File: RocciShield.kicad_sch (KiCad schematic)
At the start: 182 parts, among them J1 Battery, J10 M3, J11 I2C6, J12 M4, J13 I2C7, J14 Power, J2 I2C0, J3 I2C1, J4 I2C2, J5 I2C3, J6 M1, J7 I2C4, J8 M2, J9 I2C5, Q1 IRF7416, Q2 2N7002, U1 LMR33630, U10 LM317_TO-252, U2 LM317_TO-252, U4 TPS3700, U5 TCA9548A, U6 DRV8871, U7 DRV8871, U8 DRV8871, U9 DRV8871

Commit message: added changes from #2
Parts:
- removed C11, C12, C14, C15, C16, C17, C18, C3, C6, C8, C9: 100n, Capacitor_SMD:C_0603_1608Metric, symbol Device:C_Polarized
- removed C2: 220n, Capacitor_SMD:C_0603_1608Metric, symbol Device:C_Polarized
- removed C7: 1µ, Capacitor_SMD:CP_Elec_5x3, symbol Device:C_Polarized
- added C11, C12, C14, C15, C16, C17, C18, C19, C3, C6, C8, C9: 100n, Capacitor_SMD:C_0603_1608Metric, symbol Device:C
- added C2: 220n, Capacitor_SMD:C_0603_1608Metric, symbol Device:C
- added C7: 1µ, Capacitor_SMD:C_0603_1608Metric, symbol Device:C
- C1: value 22µ -> 33µ; footprint Capacitor_SMD:CP_Elec_5x3 -> Capacitor_Tantalum_SMD:CP_EIA-7343-43_Kemet-X; LSCL (none) -> C542504
- C10: value 22 µF -> 33µ; footprint Capacitor_SMD:CP_Elec_5x3 -> Capacitor_Tantalum_SMD:CP_EIA-7343-43_Kemet-X
- C13: value 22µ -> 33µ; footprint Capacitor_SMD:C_0603_1608Metric -> Capacitor_Tantalum_SMD:CP_EIA-7343-43_Kemet-X; LSCL (none) -> C3009395
- C4: value 22 µF -> 33µ; footprint Capacitor_SMD:CP_Elec_5x3 -> Capacitor_Tantalum_SMD:CP_EIA-7343-43_Kemet-X; LSCL C347540 -> C3009395
- C5: value 22 µF -> 33µ; footprint Capacitor_SMD:CP_Elec_5x3 -> Capacitor_Tantalum_SMD:CP_EIA-7343-43_Kemet-X; LSCL (none) -> C3009395
- D26: renamed from D31; footprint LED_SMD:LED_0603_1608Metric -> Diode_SMD:D_MiniMELF; LCSC C72043 -> C8056
- D27: renamed from D30; footprint LED_SMD:LED_0603_1608Metric -> Diode_SMD:D_MiniMELF; LCSC C72043 -> C8062
- F1: value 1 A -> 300 mA ptc; LSCL (none) -> C261938
- F10: renamed from F23; value 1 A -> 300 mA ptc
- F11: renamed from F27; value 1A -> 1A ptc; footprint Fuse:Fuse_1812_4532Metric -> Fuse:Fuse_1206_3216Metric; LSCL (none) -> C910830
- F3: renamed from F5; value 1 A -> 300 mA ptc
- F4: renamed from F8; value 1 A -> 300 mA ptc
- F5: renamed from F11; value 1 A -> 300 mA ptc
- F6: renamed from F14; value 1 A -> 300 mA ptc
- F7: renamed from F17; value 1 A -> 300 mA ptc
- F8: renamed from F20; value 1 A -> 300 mA ptc
- F9: renamed from F26; value 3A -> 3A ptc; footprint Fuse:Fuse_1812_4532Metric -> Fuse:Fuse_2920_7451Metric; LSCL (none) -> C2977527
- L1: footprint Inductor_SMD:L_6.3x6.3_H3 -> Inductor_SMD:L_Sunlord_SWPA4020S
- Q2: footprint (none) -> Package_TO_SOT_SMD:SOT-23
- R12: renamed from R44; footprint (none) -> Resistor_SMD:R_0603_1608Metric
- R13: renamed from R10; value 383k 1% -> 4700k 1%
- R15: renamed from R45; footprint (none) -> Resistor_SMD:R_0603_1608Metric
- R19: renamed from R15; value 1k47 1% -> 10k 1%
- R20: renamed from R59; footprint (none) -> Resistor_SMD:R_0603_1608Metric
- R21: renamed from R61; footprint (none) -> Resistor_SMD:R_0603_1608Metric
- R24: renamed from R58; footprint (none) -> Resistor_SMD:R_0603_1608Metric
- R25: renamed from R60; footprint (none) -> Resistor_SMD:R_0603_1608Metric
- R26: renamed from R18; value 14k3 1% -> 180k 1%
- R27: renamed from R46; footprint (none) -> Resistor_SMD:R_0603_1608Metric
- R28: renamed from R47; footprint (none) -> Resistor_SMD:R_0603_1608Metric
- R3: renamed from R42; footprint (none) -> Resistor_SMD:R_0603_1608Metric
- R31: renamed from R48; footprint (none) -> Resistor_SMD:R_0603_1608Metric
- R32: renamed from R49; footprint (none) -> Resistor_SMD:R_0603_1608Metric
- R35: renamed from R23; footprint Resistor_SMD:R_0603_1608Metric -> Resistor_SMD:R_0805_2012Metric
- R38: renamed from R50; footprint (none) -> Resistor_SMD:R_0603_1608Metric
- R39: renamed from R51; footprint (none) -> Resistor_SMD:R_0603_1608Metric
- R4: renamed from R43; footprint (none) -> Resistor_SMD:R_0603_1608Metric
- R43: renamed from R29; footprint Resistor_SMD:R_0603_1608Metric -> Resistor_SMD:R_0805_2012Metric
- R47: renamed from R52; footprint (none) -> Resistor_SMD:R_0603_1608Metric
- R48: renamed from R53; footprint (none) -> Resistor_SMD:R_0603_1608Metric
- R51: renamed from R34; footprint Resistor_SMD:R_0603_1608Metric -> Resistor_SMD:R_0805_2012Metric
- R54, R55: footprint (none) -> Resistor_SMD:R_0603_1608Metric
- R58: renamed from R39; footprint Resistor_SMD:R_0603_1608Metric -> Resistor_SMD:R_0805_2012Metric
- R61: renamed from R56; footprint (none) -> Resistor_SMD:R_0603_1608Metric
- R62: renamed from R57; footprint (none) -> Resistor_SMD:R_0603_1608Metric
- renumbered D26 to D28, D27 to D29, D28 to D30, D29 to D31, D8 to D6, D6 to D7, D7 to D8, J14 to J12, J12 to J13, J13 to J14, R8 to R10, R9 to R11, R11 to R14, R14 to R16, R12 to R17, R13 to R18, R16 to R22, R17 to R23, R19 to R29, R20 to R30, R21 to R33, R22 to R34, R24 to R36, R25 to R37, R28 to R40, R26 to R41, R27 to R42, R30 to R44, R31 to R45, R62 to R46, R32 to R49, R3 to R5, R33 to R50, R35 to R52, R36 to R53, R37 to R56, R38 to R57, R40 to R59, R4 to R6, R41 to R60, R5 to R7, R6 to R8, R7 to R9, U10 to U3
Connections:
- net +12V: now also C14.1, C15.1, C16.1, C17.1, C2.1, C9.1
- net +3V3: now also C11.1
- net +5V: now also C6.1, C8.1
- net +8V: now also C12.1, C18.1
- net 12V_after_fuse: now also C19.1
- net Boot: now also C3.1
- net GND: now also C11.2, C12.2, C14.2, C15.2, C16.2, C17.2, C18.2, C19.2, C2.2, C6.2, C7.2, C8.2, C9.2
- net SW: now also C3.2
- net at R6.1, TP4.1, U1.6 (VCC): now also C7.1
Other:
- note added: "at 10,3 V it turns off at 10,8 V it turns on again See TPS3700_Lipo_protection_calc.xlsx for reference"
- note removed: "at 10,8 V it turns off at 11 V it turns on again"

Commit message: finished JLCPCB selection and fixed isse #3
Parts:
- removed Q1: IRF7416, Package_SO:SO-8_5.3x6.2mm_P1.27mm, symbol Device:Q_PMOS_GDS
- removed Q2: 2N7002, Package_TO_SOT_SMD:SOT-23, symbol Device:Q_NMOS_GDS
- added C19: 100n, Capacitor_SMD:C_0603_1608Metric, symbol Device:C
- added Q1: IRF7404, Package_SO:SOIC-8_3.9x4.9mm_P1.27mm, symbol Transistor_FET:IRF7404
- added Q2: 2N7002, Package_TO_SOT_SMD:SOT-23, symbol Device:Q_NMOS_GSD
- added R29: 300k 1%, Resistor_SMD:R_0603_1608Metric, symbol Device:R
- added R32: 100k 1%, Resistor_SMD:R_0603_1608Metric, symbol Device:R
- C1: value 33µ -> 100µ; footprint Capacitor_Tantalum_SMD:CP_EIA-7343-43_Kemet-X -> Package_TO_SOT_SMD:SOT-23; LCSC (none) -> C962164; LSCL C542504 -> C962164
- C10: renamed from C11; LCSC (none) -> C14663
- C11: renamed from C10; value 33µ -> 100µ; footprint Capacitor_Tantalum_SMD:CP_EIA-7343-43_Kemet-X -> Capacitor_SMD:CP_Elec_6.3x7.7; LCSC (none) -> C962164; LSCL (none) -> C962164
- C12: renamed from C9; LCSC (none) -> C14663
- C13: renamed from C12; LCSC (none) -> C14663
- C14: renamed from C13; value 33µ -> 100µ; footprint Capacitor_Tantalum_SMD:CP_EIA-7343-43_Kemet-X -> Capacitor_SMD:CP_Elec_6.3x7.7; LCSC (none) -> C962164; LSCL C3009395 -> C962164
- C15: renamed from C14; LCSC (none) -> C14663
- C16: renamed from C15; LCSC (none) -> C14663
- C17: renamed from C16; LCSC (none) -> C14663
- C18: renamed from C17; LCSC (none) -> C14663
- C2: LCSC (none) -> C21120
- C20: renamed from C18; LCSC (none) -> C14663
- C3, C6: LCSC (none) -> C14663
- C4, C5: LCSC (none) -> C3009395
- C7: LCSC (none) -> C15849
- C8: renamed from C19; LCSC (none) -> C14663
- C9: renamed from C8; LCSC (none) -> C14663
- F1, F10, F3, F4, F5, F6, F7, F8: LCSC (none) -> C261938
- F11: LCSC (none) -> C910830
- F9: LCSC (none) -> C2977527
- R1, R10, R11, R2, R22, R23, R8, R9: LCSC (none) -> C23162
- R12, R15, R27, R28, R3, R4: LCSC (none) -> C22775
- R13: LCSC (none) -> C23163
- R14, R19: LCSC (none) -> C25804
- R16: LCSC (none) -> C1603
- R17: LCSC (none) -> C23138
- R18: LCSC (none) -> C22808
- R20, R21: LCSC (none) -> C23350
- R24: LCSC (none) -> C23151
- R25: LCSC (none) -> C22767
- R26: LCSC (none) -> C22827
- R30: renamed from R29; LCSC (none) -> C23162
- R31: renamed from R30; LCSC (none) -> C23162
- R33: renamed from R31; LCSC (none) -> C22775
- R34: renamed from R32; LCSC (none) -> C22775
- R35: renamed from R33; LCSC (none) -> C1603
- R36: renamed from R34; LCSC (none) -> C1603
- R37: renamed from R35; LCSC (none) -> C22984
- R38: renamed from R36; LCSC (none) -> C23162
- R39: renamed from R37; LCSC (none) -> C23162
- R40: renamed from R38; LCSC (none) -> C22775
- R41: renamed from R39; LCSC (none) -> C22775
- R42: renamed from R40; LCSC (none) -> C22966
- R43: renamed from R41; LCSC (none) -> C1603
- R44: renamed from R42; LCSC (none) -> C1603
- R45: renamed from R43; LCSC (none) -> C22984
- R46: renamed from R44; LCSC (none) -> C23162
- R47: renamed from R45; LCSC (none) -> C23162
- R48: renamed from R46; value 1k -> 10k; LCSC (none) -> C25804
- R49: renamed from R47; LCSC (none) -> C22775
- R5, R6: LCSC (none) -> C25803
- R50: renamed from R48; LCSC (none) -> C22775
- R51: renamed from R49; LCSC (none) -> C1603
- R52: renamed from R50; LCSC (none) -> C1603
- R53: renamed from R51; LCSC (none) -> C22984
- R54: renamed from R52; LCSC (none) -> C23162
- R55: renamed from R53; LCSC (none) -> C23162
- R56: renamed from R54; LCSC (none) -> C22775
- R57: renamed from R55; LCSC (none) -> C22775
- R58: renamed from R56; LCSC (none) -> C1603
- R59: renamed from R57; LCSC (none) -> C1603
- R60: renamed from R58; LCSC (none) -> C22984
- R61: renamed from R59; LCSC (none) -> C23162
- R62: renamed from R60; LCSC (none) -> C23162
- R63: renamed from R61; LCSC (none) -> C22775
- R64: renamed from R62; LCSC (none) -> C22775
- R7: LCSC (none) -> C25962
- U2, U3: LCSC (none) -> C75510
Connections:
- net 12V_after_fuse is gone; now on net +12V: C8.1, D3.1 (K), F2.2, R13.1, R14.1, TP7.1, U4.5 (VDD)
- net +12V: now also Q1.5 (D), Q1.6 (D), Q1.7 (D), Q1.8 (D); no longer C1.1, C12.1, C2.1, D6.2 (A), U1.2 (VIN), U1.3 (EN), U3.3 (VI)
- net ADC_BAT: now also C19.2, R29.2, R32.1; no longer R13.2, R19.1, U4.3 (INA+)
- net ERROR_LED: now also Q2.1 (G)
- net GND: now also C19.1, Q2.3 (D), R32.2
- net at R14.2, TP13.1, U4.6 (OUTB): now also Q1.4 (G)
- net at R42.2: now also Q2.2 (S)
- new net: R13.2, R19.1, U4.3 (INA+)
- new net +12VA: C1.1, C12.1, C2.1, D6.2 (A), Q1.1 (S), Q1.2 (S), Q1.3 (S), R29.1, U1.2 (VIN), U1.3 (EN), U3.3 (VI)
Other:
- note added: "25V 50mΩ"
- note added: "3.15V @ 12.6 V 2.6V @ 10.4 V with VREF=5V -> span=110 ADU with VREF=3.3V -> span=167 ADU"
- note added: "30mΩ 5.2A"
- note added: "50V 340mΩ"
- note added: "TODO: - is the power connector large enough? - do we need max motor current?"
- note removed: "TODO: - select components for switching regulator - define netclasses - is the power connector large enough? - do we need max motor current? - add freerunning diodes"
- moved on the sheet: C2, C8

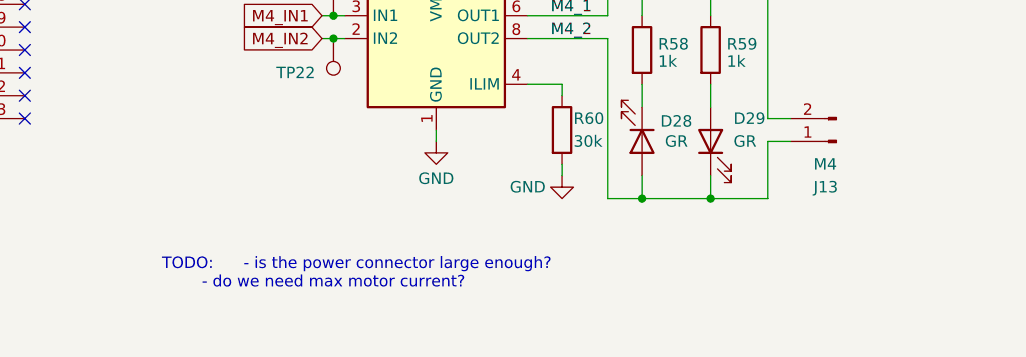
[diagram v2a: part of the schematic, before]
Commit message: added more TODOs
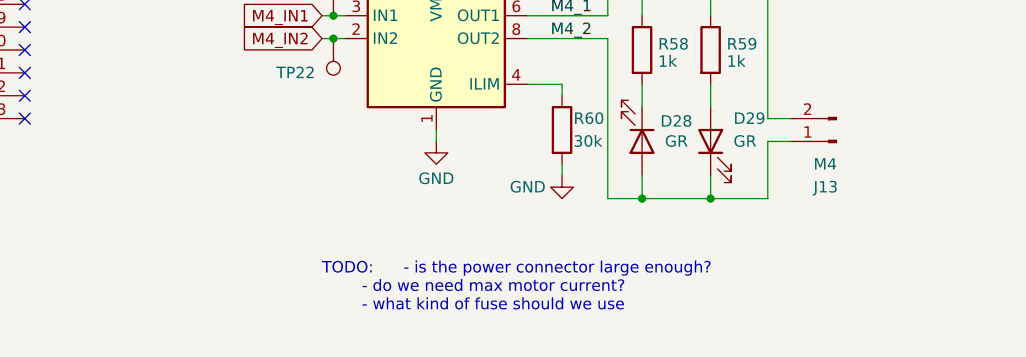
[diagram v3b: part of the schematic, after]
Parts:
- F2: LCSC (none) -> C122783
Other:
- note added: "TODO: - is the power connector large enough? - do we need max motor current? - what kind of fuse should we use"
- note removed: "TODO: - is the power connector large enough? - do we need max motor current?"
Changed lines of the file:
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@@
     (title "RoCCI Shield")
     (date "2023-06-27")
-    (rev "0.5")
+    (rev "0.6")
     (company "RoCCI e.V.")
   )
@@
     (effects (font (size 3 3)) (justify left bottom))
   )
-  (text "TODO:  	- is the power connector large enough?\n		- do we need max motor current?"
-    (at 302.26 257.81 0)
+  (text "TODO:  	- is the power connector large enough?\n		- do we need max motor current?\n		- what kind of fuse should we use "
+    (at 320.04 260.35 0)
     (effects (font (size 1.27 1.27)) (justify left bottom))
   )
@@
       (effects (font (size 1.27 1.27)) hide)
     )
+    (property "LCSC" "C122783" (at 213.36 34.29 90)
+      (effects (font (size 1.27 1.27)) hide)
+    )

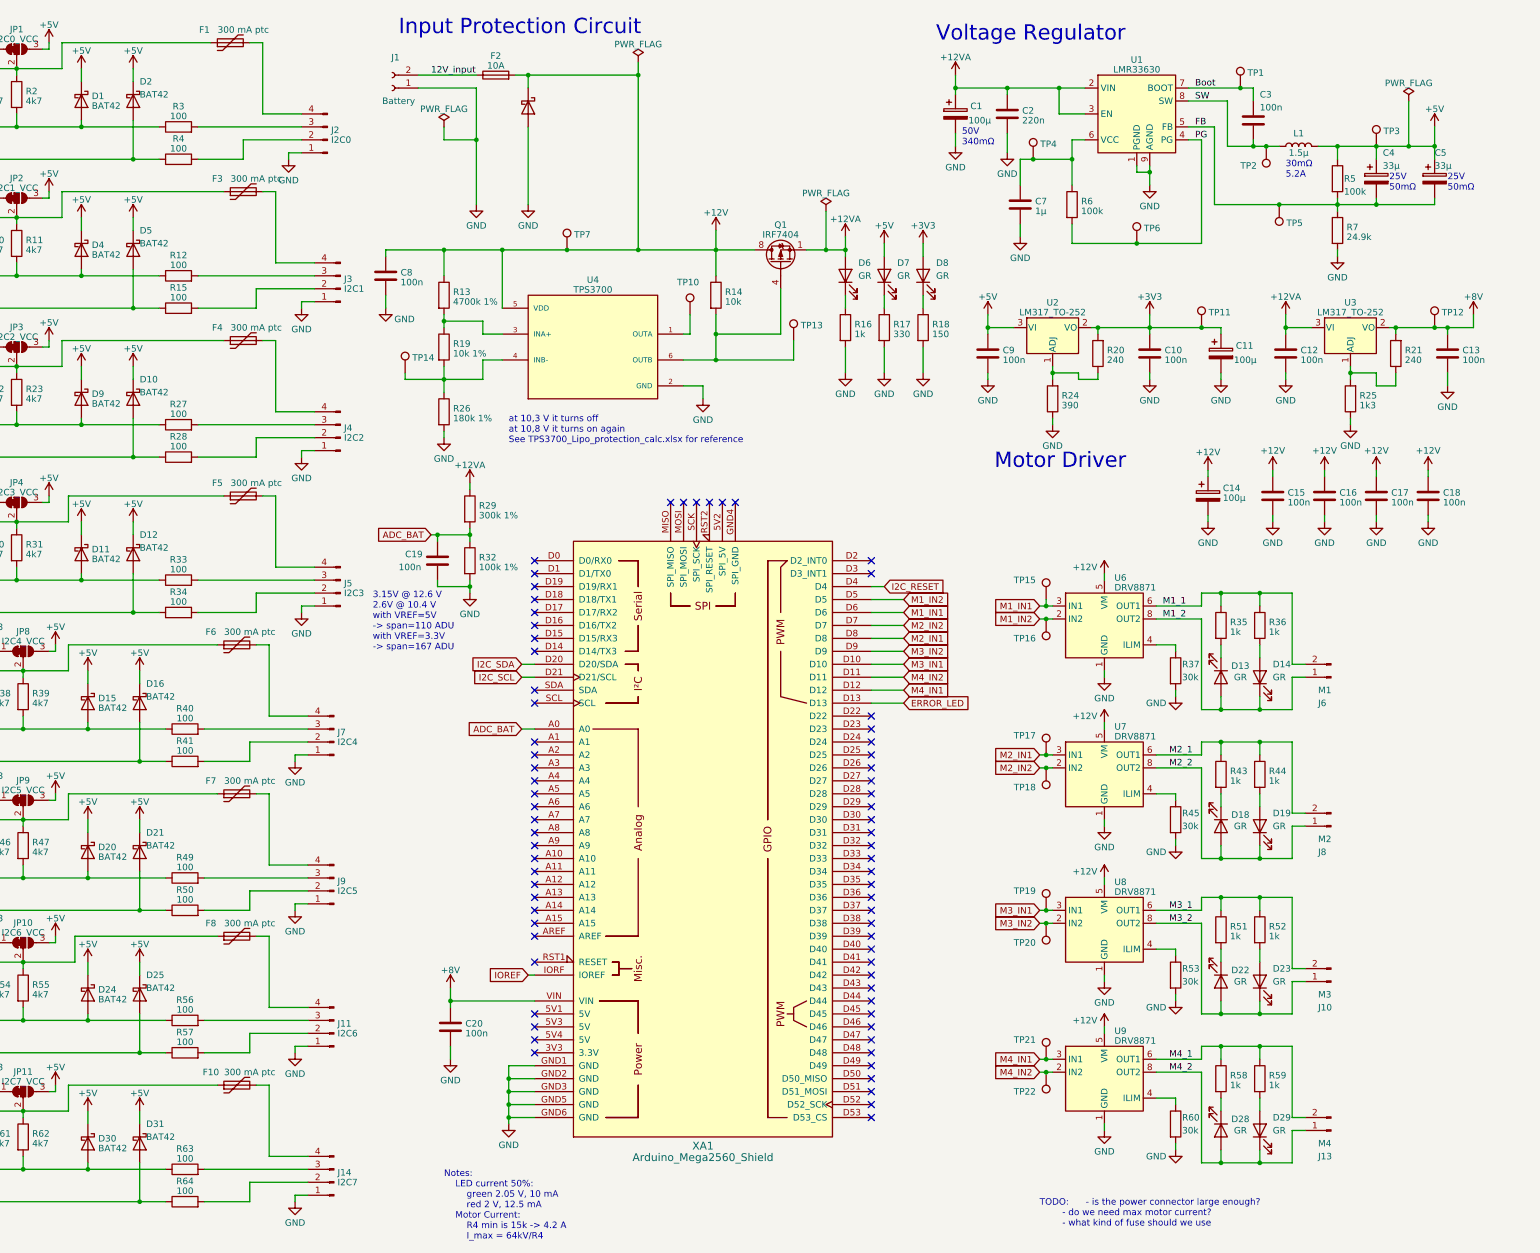
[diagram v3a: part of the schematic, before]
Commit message: first placment finished. Needs some adjustment
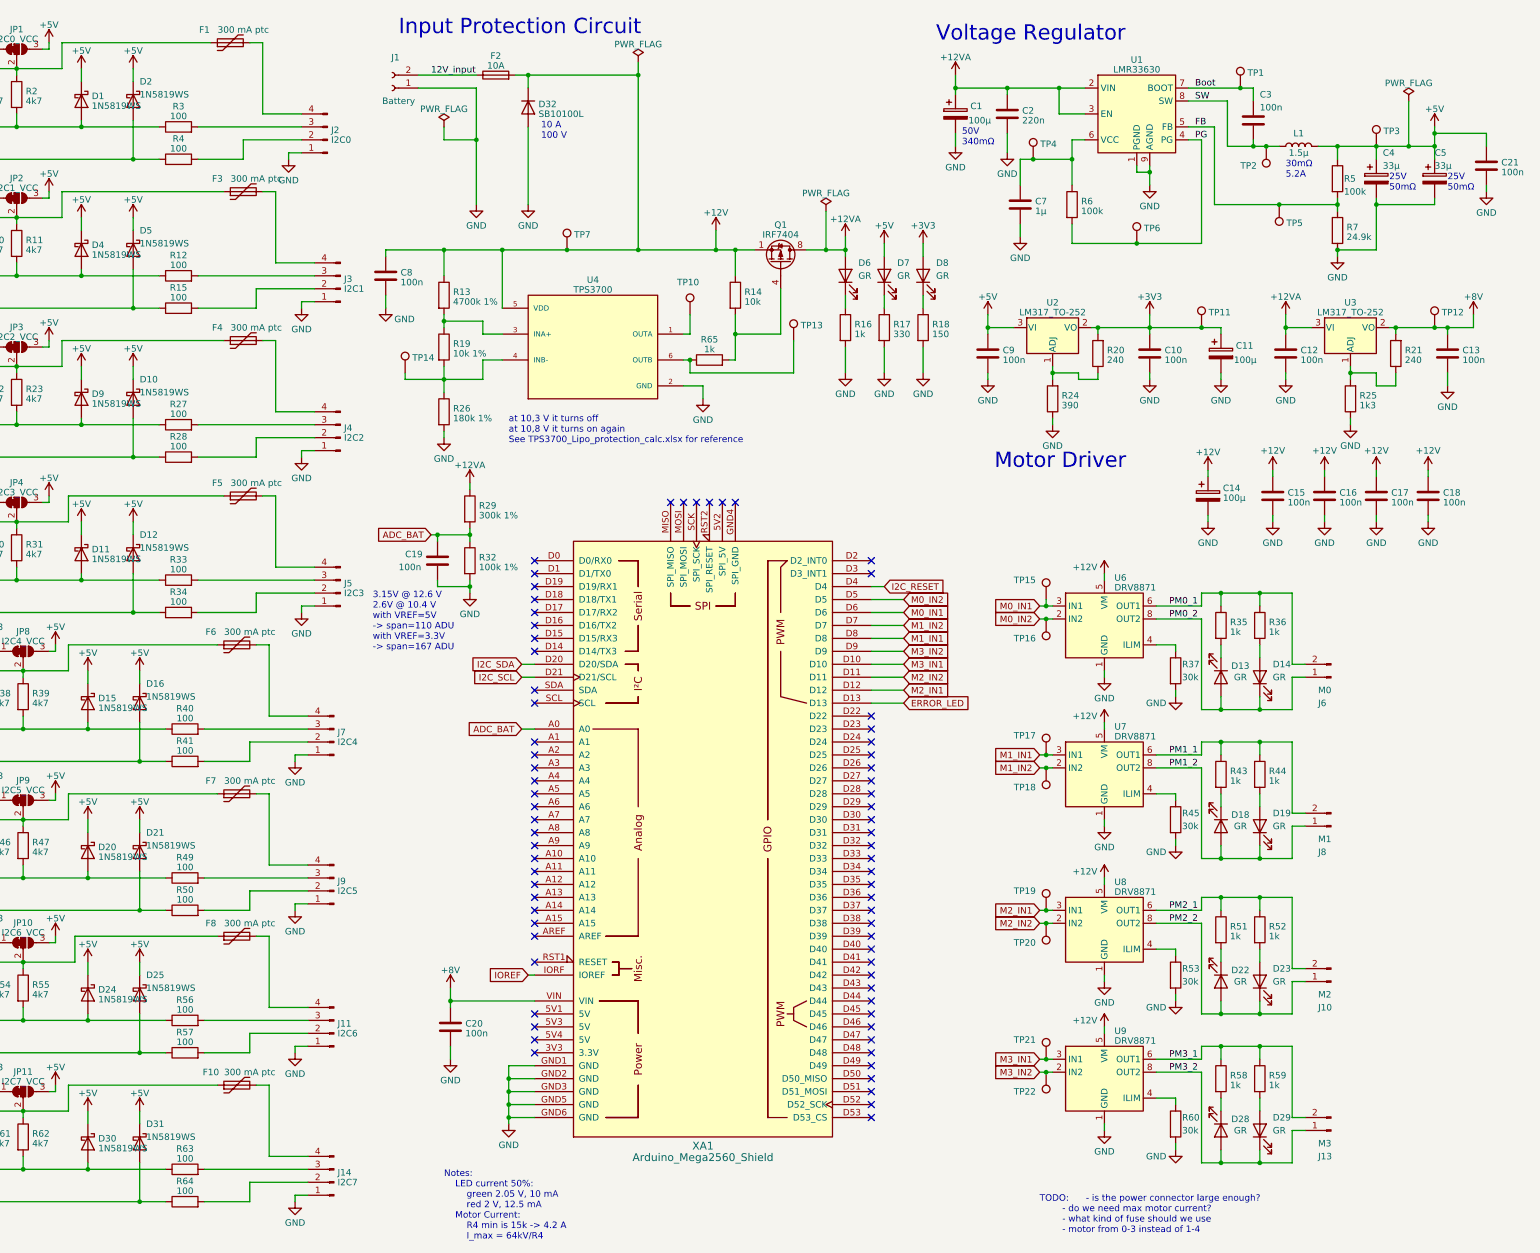
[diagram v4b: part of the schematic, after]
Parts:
- removed D3: CDBA340-HF, Diode_SMD:D_SMA, symbol Diode:CDBA340-HF
- added C21: 100n, Capacitor_SMD:C_0603_1608Metric, symbol Device:C
- added D32: SB10100L, Package_TO_SOT_SMD:TO-277A, symbol Diode:VS-6ESU06
- added R65: 1k, Resistor_SMD:R_0603_1608Metric, symbol Device:R
- C1: footprint Package_TO_SOT_SMD:SOT-23 -> Capacitor_SMD:CP_Elec_6.3x7.7
- D1, D10, D11, D12, D15, D16, D2, D20, D21, D24, D25, D30, D31, D4, D5, D9: value BAT42 -> 1N5819WS; footprint Diode_SMD:D_SOD-123 -> Diode_SMD:D_SOD-323; LCSC C8598 -> C191023
- F2: footprint Fuse:Fuse_0805_2012Metric -> Fuse:Fuseholder_Cylinder-5x20mm_Wuerth_696103101002-SMD_Horizontal_Open
- J1: footprint Connector_AMASS:AMASS_XT30U-M_1x02_P5.0mm_Vertical -> Connector_Phoenix_MSTB:PhoenixContact_MSTBVA_2,5_2-G_1x02_P5.00mm_Vertical
- J10: value M3 -> M2
- J13: value M4 -> M3
- J6: value M1 -> M0
- J8: value M2 -> M1
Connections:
- net +12V: now also Q1.1 (S), Q1.2 (S), Q1.3 (S), D32.3 (K); no longer Q1.5 (D), Q1.6 (D), Q1.7 (D), Q1.8 (D)
- net +12VA: now also Q1.5 (D), Q1.6 (D), Q1.7 (D), Q1.8 (D); no longer Q1.1 (S), Q1.2 (S), Q1.3 (S)
- net +5V: now also C21.1
- net FB: no longer C4.2, C5.2
- net GND: now also C4.2, C5.2, C21.2, D32.1 (A), D32.2 (A)
- net M1_IN1: now also TP17.1, U7.3 (IN1), XA1.D8; no longer TP15.1, U6.3 (IN1), XA1.D6
- net M1_IN2: now also TP18.1, U7.2 (IN2), XA1.D7; no longer TP16.1, U6.2 (IN2), XA1.D5
- net M2_IN1: now also TP19.1, U8.3 (IN1), XA1.D12; no longer TP17.1, U7.3 (IN1), XA1.D8
- net M2_IN2: now also TP20.1, U8.2 (IN2), XA1.D11; no longer TP18.1, U7.2 (IN2), XA1.D7
- net M3_IN1: now also TP21.1, U9.3 (IN1); no longer TP19.1, U8.3 (IN1)
- net M3_IN2: now also TP22.1, U9.2 (IN2); no longer TP20.1, U8.2 (IN2)
- net at Q1.4 (G), R14.2: now also R65.2; no longer TP13.1, U4.6 (OUTB)
- net M1_1 renamed PM0_1
- net M1_2 renamed PM0_2
- net M2_1 renamed PM1_1
- net M2_2 renamed PM1_2
- net M3_1 renamed PM2_1
- net M3_2 renamed PM2_2
- net M4_1 renamed PM3_1
- net M4_2 renamed PM3_2
- removed net M4_IN1: TP21.1, U9.3 (IN1), XA1.D12
- removed net M4_IN2: TP22.1, U9.2 (IN2), XA1.D11
- new net: R65.1, TP13.1, U4.6 (OUTB)
- new net M0_IN1: TP15.1, U6.3 (IN1), XA1.D6
- new net M0_IN2: TP16.1, U6.2 (IN2), XA1.D5
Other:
- note added: "10 A 100 V"
- note added: "TODO: - is the power connector large enough? - do we need max motor current? - what kind of fuse should we use - motor from 0-3 instead of 1-4"
- note removed: "TODO: - is the power connector large enough? - do we need max motor current? - what kind of fuse should we use"
- moved on the sheet: Q1, R14
